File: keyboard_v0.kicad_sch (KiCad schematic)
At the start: 2 parts, among them U1 ATmega32U4-A

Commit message: Reinitialize
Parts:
- removed R1: 10k, symbol Device:R_Small
- removed U1: ATmega32U4-A, Package_QFP:TQFP-44_10x10mm_P0.8mm, symbol MCU_Microchip_ATmega:ATmega32U4-A

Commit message: Update MCU schematic
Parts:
- added C1: 1uF, symbol Device:C_Small
- added C2, C3: 22pF, symbol Device:C_Small
- added C4, C5, C6, C7: 0.1uF, symbol Device:C_Small
- added C8: 10uF, symbol Device:C_Small
- added F1: 500m, symbol Device:Polyfuse_Small
- added J1: AVR-ISP-6, symbol Connector:AVR-ISP-6
- added J2: USB_C_Receptacle_USB2.0_16P, symbol Connector:USB_C_Receptacle_USB2.0_16P
- added R1: 10k, symbol Device:R_Small
- added R2: R_Small, symbol Device:R_Small
- added R3, R4: 22, symbol Device:R_Small
- added R5, R6: 5.1k, symbol Device:R_Small
- added SW1: SW_RESET, symbol Keeb_Library:SW_SPST_NO
- added U1: ATmega32U4-A, Package_QFP:TQFP-44_10x10mm_P0.8mm, symbol MCU_Microchip_ATmega:ATmega32U4-A
- added U2: USBLC6-2P6, Package_TO_SOT_SMD:SOT-666, symbol Power_Protection:USBLC6-2P6
- added Y1: Crystal_GND24_Small, symbol Device:Crystal_GND24_Small
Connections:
- new net: J2.A6 (D+), J2.B6 (D+), R4.1, U2.1 (I/O1), U2.6 (I/O1)
- new net: C1.1, U1.6 (UCAP)
- new net: J2.A7 (D-), J2.B7 (D-), R3.1, U2.3 (I/O2), U2.4 (I/O2)
- new net: J2.A5 (CC1), R5.1
- new net: R1.1, U1.33 (~{HWB}/PE2)
- new net: J2.B5 (CC2), R6.1
- new net +5V: C4.1, C5.1, C6.1, C7.1, C8.1, F1.2, J1.2 (VCC), R2.2, U1.14 (VCC), U1.2 (UVCC), U1.24 (AVCC), U1.34 (VCC), U1.44 (AVCC), U1.7 (VBUS)
- new net D+: R4.2, U1.4 (D+)
- new net D-: R3.2, U1.3 (D-)
- new net GND: C1.2, C2.2, C3.2, C4.2, C5.2, C6.2, C7.2, C8.2, J1.6 (GND), J2.A1 (GND), J2.A12 (GND), J2.B1 (GND), J2.B12 (GND), J2.SH (SHIELD), R1.2, R5.2, R6.2, SW1.2 (K), U1.15 (GND), U1.23 (GND), U1.35 (GND), U1.43 (GND), U1.5 (UGND), U2.2 (GND), Y1.2 (G), Y1.4 (G)
- new net PICO: J1.4 (MOSI), U1.10 (PB2)
- new net POCI: J1.1 (MISO), U1.11 (PB3)
- new net RESET: J1.5 (~{RST}), R2.1, SW1.4 (2), U1.13 (~{RESET})
- new net SCK: J1.3 (SCK), U1.9 (PB1)
- new net VCC: F1.1, J2.A4 (VBUS), J2.A9 (VBUS), J2.B4 (VBUS), J2.B9 (VBUS), U2.5 (VBUS)
- new net XTAL1: C2.1, U1.17 (XTAL1), Y1.1
- new net XTAL2: C3.1, U1.16 (XTAL2), Y1.3
- no-connect marks 0 -> 28

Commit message: Complete switch matrix
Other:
- added sheet Matrix (matrix.kicad_sch)
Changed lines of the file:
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@@
+		)
+	)
+	(sheet
+		(at 31.115 146.05)
+		(size 29.845 15.24)
+		(exclude_from_sim no)
+		(in_bom yes)
+		(on_board yes)
+		(dnp no)
+		(fields_autoplaced yes)
+		(stroke
+			(width 0.1524)
+			(type solid)
+		)
+		(fill
+			(color 0 0 0 0)
+		)
+		(property "Sheetname" "Matrix"
+			(at 31.115 145.3384 0)
+			(show_name no)
+			(do_not_autoplace no)
+			(effects
+				(font
+					(size 1.27 1.27)
+				)
+				(justify left bottom)
+			)
+		)
+		(property "Sheetfile" "matrix.kicad_sch"
+			(at 31.115 161.8746 0)
+			(show_name no)
+			(do_not_autoplace no)
+			(effects
+				(font
+					(size 1.27 1.27)
+				)
+				(justify left top)
+			)
+		)
+		(instances
+			(project "keyboard_v0"
+				(path "/8362a6cf-ebff-48ab-839d-27af3298a826"
+					(page "2")
+				)
+			)
 		)
 	)

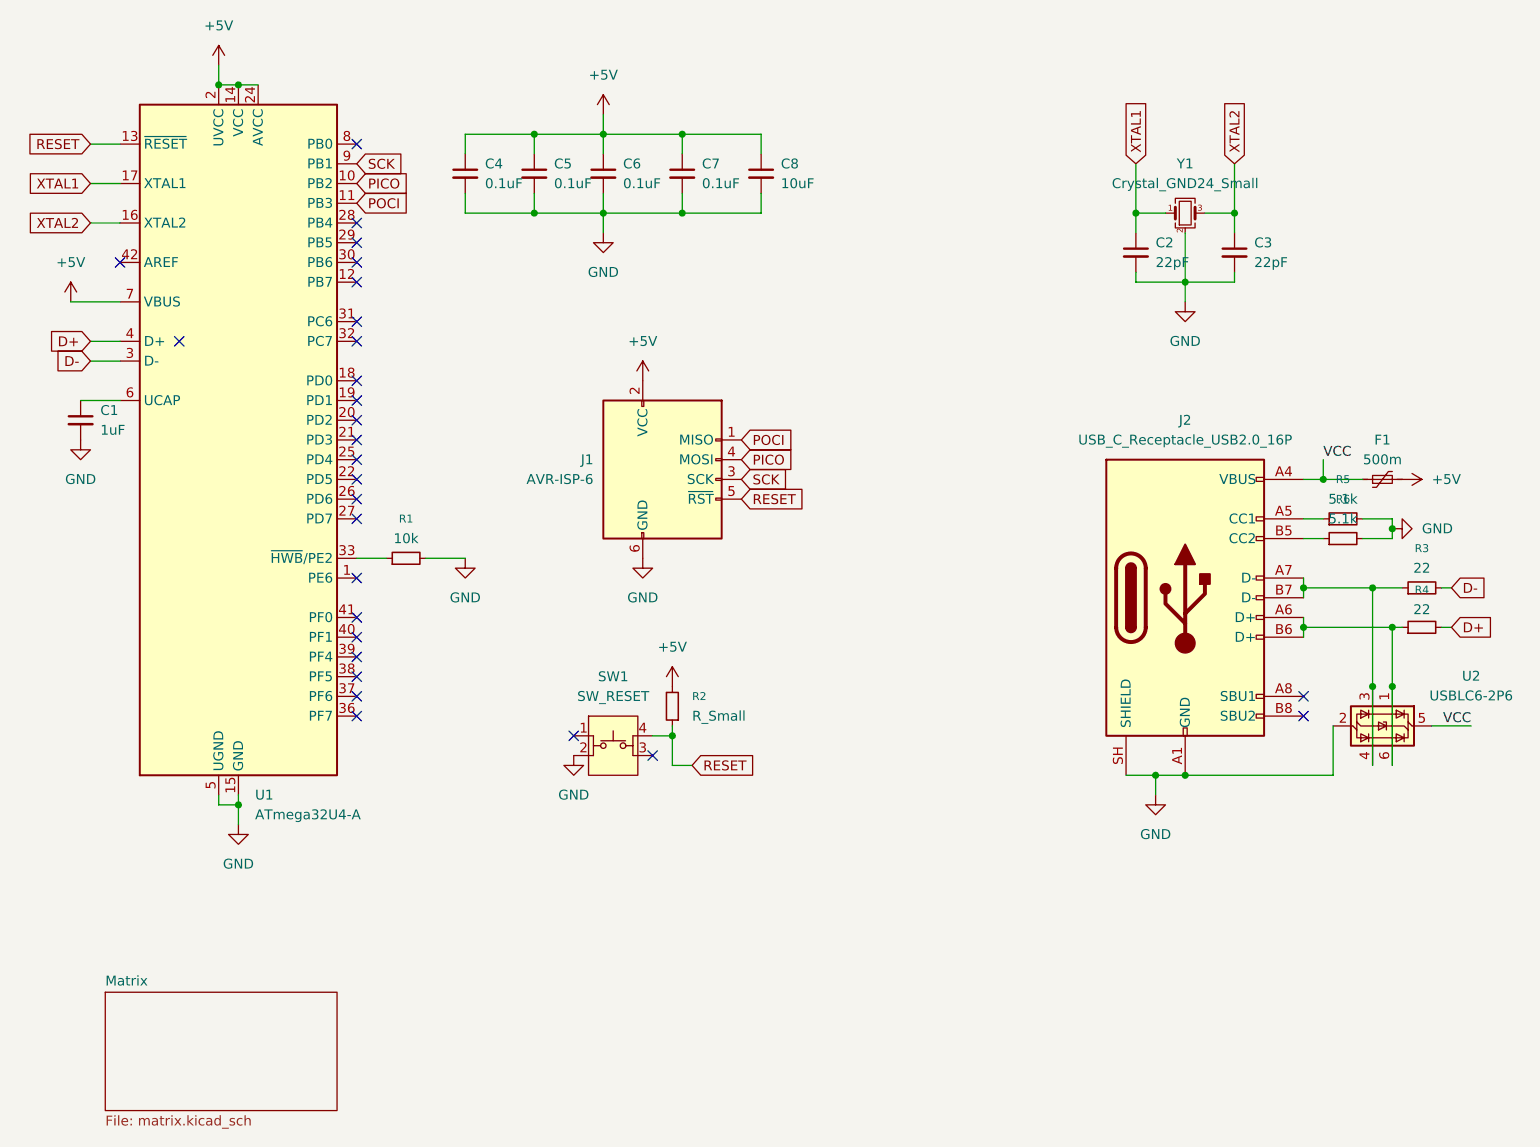
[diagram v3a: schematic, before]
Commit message: Connected matrix to MCU
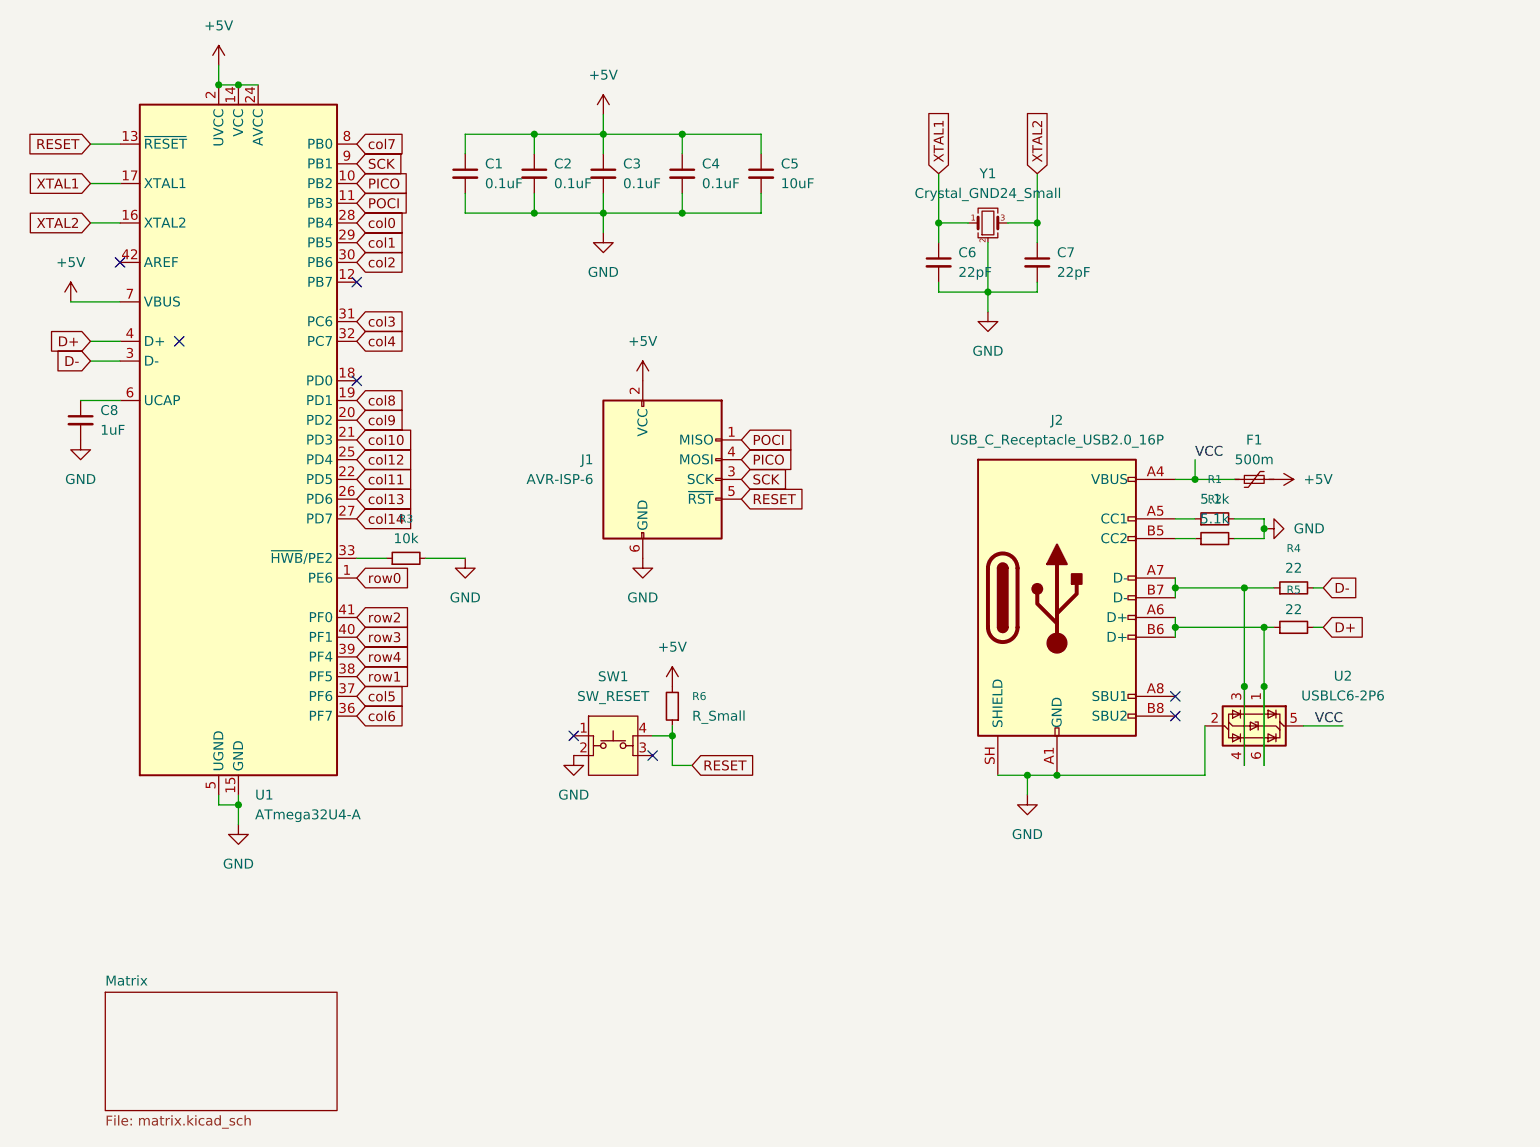
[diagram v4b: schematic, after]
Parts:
- renumbered C4 to C1, C5 to C2, C6 to C3, C7 to C4, C8 to C5, C2 to C6, C3 to C7, C1 to C8, R5 to R1, R6 to R2, R1 to R3, R3 to R4, R4 to R5, R2 to R6
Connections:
- net row0: now reaches U1.1 (PE6)
- net col8: now reaches U1.19 (PD1)
- net col9: now reaches U1.20 (PD2)
- net col10: now reaches U1.21 (PD3)
- net col11: now reaches U1.22 (PD5)
- net col12: now reaches U1.25 (PD4)
- net col13: now reaches U1.26 (PD6)
- net col14: now reaches U1.27 (PD7)
- net col0: now reaches U1.28 (PB4)
- net col1: now reaches U1.29 (PB5)
- net col2: now reaches U1.30 (PB6)
- net col3: now reaches U1.31 (PC6)
- net col4: now reaches U1.32 (PC7)
- net col6: now reaches U1.36 (PF7)
- net col5: now reaches U1.37 (PF6)
- net row1: now reaches U1.38 (PF5)
- net row4: now reaches U1.39 (PF4)
- net row3: now reaches U1.40 (PF1)
- net row2: now reaches U1.41 (PF0)
- net col7: now reaches U1.8 (PB0)
- no-connect marks 28 -> 8
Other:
- moved on the sheet: C6, C7, F1, J2, R1, R2, R4, R5, U2, Y1

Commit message: Power flags
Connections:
- no-connect marks 8 -> 7

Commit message: Footprint assignment
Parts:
- C1, C2, C3, C4, C5, C6, C7, C8: footprint (none) -> Capacitor_SMD:C_0805_2012Metric_Pad1.18x1.45mm_HandSolder
- F1: footprint (none) -> Fuse:Fuse_1206_3216Metric_Pad1.42x1.75mm_HandSolder
- J1: footprint (none) -> random-keyboard-parts:Reset_Pretty-Mask
- J2: footprint (none) -> UJ20-C-H-G-SMT-1-P16-TR:SAMESKY_UJ20-C-H-G-SMT-1-P16-TR
- R1, R2, R3, R4, R5, R6: footprint (none) -> Resistor_SMD:R_0805_2012Metric_Pad1.20x1.40mm_HandSolder
- SW1: footprint (none) -> Button_Switch_SMD:SW_SPST_SKQG_WithStem
- Y1: footprint (none) -> Crystal:Crystal_SMD_3225-4Pin_3.2x2.5mm_HandSoldering
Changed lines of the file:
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@@
 			)
 		)
-		(property "Footprint" ""
+		(property "Footprint" "Fuse:Fuse_1206_3216Metric_Pad1.42x1.75mm_HandSolder"
 			(at 184.15 78.74 0)
 			(hide yes)
@@
 			)
 		)
-		(property "Footprint" ""
+		(property "Footprint" "random-keyboard-parts:Reset_Pretty-Mask"
 			(at 96.52 78.74 90)
 			(hide yes)
@@
 			)
 		)
-		(property "Footprint" ""
+		(property "Footprint" "Resistor_SMD:R_0805_2012Metric_Pad1.20x1.40mm_HandSolder"
 			(at 104.14 109.22 0)
 			(hide yes)
@@
 			)
 		)
-		(property "Footprint" ""
+		(property "Footprint" "Capacitor_SMD:C_0805_2012Metric_Pad1.18x1.45mm_HandSolder"
 			(at 95.25 40.64 0)
 			(hide yes)
@@
 			)
 		)
-		(property "Footprint" ""
+		(property "Footprint" "Capacitor_SMD:C_0805_2012Metric_Pad1.18x1.45mm_HandSolder"
 			(at 115.57 40.64 0)
 			(hide yes)
@@
 			)
 		)
-		(property "Footprint" ""
+		(property "Footprint" "Capacitor_SMD:C_0805_2012Metric_Pad1.18x1.45mm_HandSolder"
 			(at 105.41 40.64 0)
 			(hide yes)
@@
 			)
 		)
-		(property "Footprint" ""
+		(property "Footprint" "Capacitor_SMD:C_0805_2012Metric_Pad1.18x1.45mm_HandSolder"
 			(at 138.43 52.07 0)
 			(hide yes)
@@
 			)
 		)
-		(property "Footprint" ""
+		(property "Footprint" "Resistor_SMD:R_0805_2012Metric_Pad1.20x1.40mm_HandSolder"
 			(at 184.15 99.06 0)
 			(hide yes)
@@
 			)
 		)
-		(property "Footprint" ""
+		(property "Footprint" "Capacitor_SMD:C_0805_2012Metric_Pad1.18x1.45mm_HandSolder"
 			(at 27.94 72.39 0)
 			(hide yes)
@@
 			)
 		)
-		(property "Footprint" ""
+		(property "Footprint" "Resistor_SMD:R_0805_2012Metric_Pad1.20x1.40mm_HandSolder"
 			(at 184.15 93.98 0)
 			(hide yes)
@@
 			)
 		)
-		(property "Footprint" ""
+		(property "Footprint" "Resistor_SMD:R_0805_2012Metric_Pad1.20x1.40mm_HandSolder"
 			(at 173.99 85.09 0)
 			(hide yes)
@@
 			)
 		)
-		(property "Footprint" ""
+		(property "Footprint" "Crystal:Crystal_SMD_3225-4Pin_3.2x2.5mm_HandSoldering"
 			(at 144.78 46.99 0)
 			(hide yes)
@@
 			)
 		)
-		(property "Footprint" ""
+		(property "Footprint" "Resistor_SMD:R_0805_2012Metric_Pad1.20x1.40mm_HandSolder"
 			(at 173.99 87.63 0)
 			(hide yes)
@@
 			)
 		)
-		(property "Footprint" ""
+		(property "Footprint" "Resistor_SMD:R_0805_2012Metric_Pad1.20x1.40mm_HandSolder"
 			(at 69.85 90.17 0)
 			(hide yes)
@@
 			)
 		)
-		(property "Footprint" ""
+		(property "Footprint" "Capacitor_SMD:C_0805_2012Metric_Pad1.18x1.45mm_HandSolder"
 			(at 151.13 52.07 0)
 			(hide yes)
@@
 			)
 		)
-		(property "Footprint" ""
+		(property "Footprint" "Button_Switch_SMD:SW_SPST_SKQG_WithStem"
 			(at 96.52 107.95 0)
 			(hide yes)
@@
 			)
 		)
-		(property "Footprint" ""
+		(property "Footprint" "UJ20-C-H-G-SMT-1-P16-TR:SAMESKY_UJ20-C-H-G-SMT-1-P16-TR"
 			(at 157.48 95.25 0)
 			(hide yes)
@@
 			)
 		)
-		(property "Footprint" ""
+		(property "Footprint" "Capacitor_SMD:C_0805_2012Metric_Pad1.18x1.45mm_HandSolder"
 			(at 77.47 40.64 0)
 			(hide yes)
@@
 			)
 		)
-		(property "Footprint" ""
+		(property "Footprint" "Capacitor_SMD:C_0805_2012Metric_Pad1.18x1.45mm_HandSolder"
 			(at 86.36 40.64 0)
 			(hide yes)

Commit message: Fixed footprint and symbol mismatch
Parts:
- removed J2: USB_C_Receptacle_USB2.0_16P, UJ20-C-H-G-SMT-1-P16-TR:SAMESKY_UJ20-C-H-G-SMT-1-P16-TR, symbol Connector:USB_C_Receptacle_USB2.0_16P
- added J3: UJ20-C-H-G-SMT-1-P16-TR, UJ20-C-H-G-SMT-1-P16-TR:SAMESKY_UJ20-C-H-G-SMT-1-P16-TR, symbol UJ20-C-H-G-SMT-1-P16-TR:UJ20-C-H-G-SMT-1-P16-TR
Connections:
- net GND: now also J3.A1_B12 (GND), J3.B1_A12 (GND), J3.SH1 (SHIELD), J3.SH2 (SHIELD), J3.SH3 (SHIELD), J3.SH4 (SHIELD)
- net RESET: now also SW1.1 (A); no longer SW1.4 (2)
- net VCC: now also J3.A4_B9 (VBUS), J3.B4_A9 (VBUS)
- net at U2.1 (I/O1), U2.6 (I/O1): no longer R5.1
- net at U2.3 (I/O2), U2.4 (I/O2): no longer R4.1
- net at R1.1: now also J3.A5 (CC1)
- net at R2.1: now also J3.B5 (CC2)
- new net: J3.A6 (DP1), J3.B6 (DP2), R5.1
- new net: J3.A7 (DN1), J3.B7 (DN2), R4.1
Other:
- moved on the sheet: F1, R1, R2, R4, R5, U2

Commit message: Complete routing
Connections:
- net col5: now also U1.36 (PF7); no longer U1.37 (PF6)
- net col6: now also U1.37 (PF6); no longer U1.36 (PF7)
- net row1: now also U1.39 (PF4); no longer U1.38 (PF5)
- net row2: now also U1.40 (PF1); no longer U1.41 (PF0)
- net row3: now also U1.41 (PF0); no longer U1.40 (PF1)
- net row4: now also U1.38 (PF5); no longer U1.39 (PF4)
- net DP: now reaches J3.A6 (DP1), J3.B6 (DP2)
- net DP: now also U2.3 (I/O2); no longer R5.1
- net DN: now reaches J3.A7 (DN1), J3.B7 (DN2)
- net DN: now also U2.1 (I/O1); no longer R4.1
- net at U2.6 (I/O1): now also R4.1; no longer U2.1 (I/O1)
- net at U2.4 (I/O2): now also R5.1; no longer U2.3 (I/O2)
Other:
- moved on the sheet: R4, R5, U2
